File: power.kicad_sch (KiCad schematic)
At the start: 0 parts

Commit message: added symbols
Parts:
- added U4: ~, symbol sumo-robot-symbols:RS3E075AT
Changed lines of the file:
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@@
 	(generator_version "9.0")
 	(paper "A4")
+	(symbol
+		(lib_id "sumo-robot-symbols:RS3E075AT")
+		(at 129.54 82.55 0)
+		(unit 1)
+		(exclude_from_sim no)
+		(in_bom yes)
+		(on_board yes)
+		(dnp no)
+		(property "Reference" "U4"
+			(at 130.302 69.596 0)
+			(effects
+				(font
+					(size 1.27 1.27)
+				)
+			)
+		)
+		(property "Value" "~"
+			(at 137.16 67.31 0)
+			(effects
+				(font
+					(size 1.27 1.27)
+				)
+			)
+		)
+		(property "Footprint" ""
+			(at 129.54 82.55 0)
+			(effects
+				(font
+					(size 1.27 1.27)
+				)
+				(hide yes)
+			)
+		)
+		(property "Datasheet" ""
+			(at 129.54 82.55 0)
+			(effects
+				(font
+					(size 1.27 1.27)
+				)
+				(hide yes)
+			)
+		)
+		(property "Description" ""
+			(at 129.54 82.55 0)
+			(effects
+				(font
+					(size 1.27 1.27)
+				)
+				(hide yes)
+			)
+		)
+		(pin "2"
+		)
+		(pin "3"
+		)
+		(pin "4"
+		)
+		(pin "8"
+		)
+		(pin "7"
+		)
+		(pin "6"
+		)
+		(pin "5"
+		)
+		(pin "1"
+		)
+		(instances
+			(project ""
+				(path "/f283bc71-7763-4093-b75c-cbe2f5868c12/4425b7fb-6f26-4a13-b5c2-41b1a59df573"
+					(reference "U4")
+					(unit 1)
+				)
+			)
+		)
+	)
 )

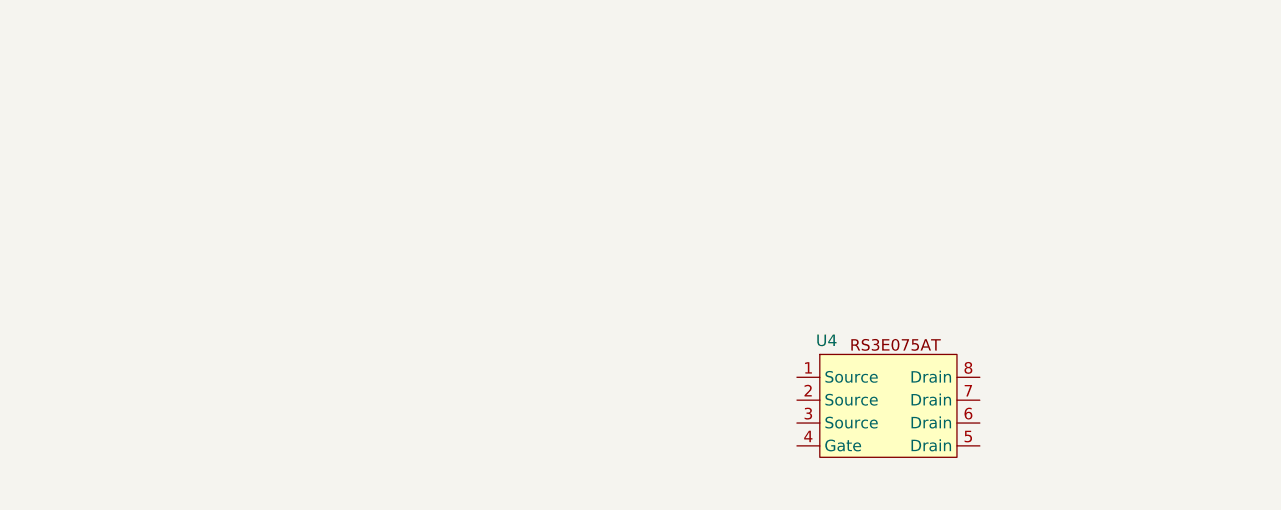
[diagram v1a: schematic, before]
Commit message: added power connectors and modified power shematic
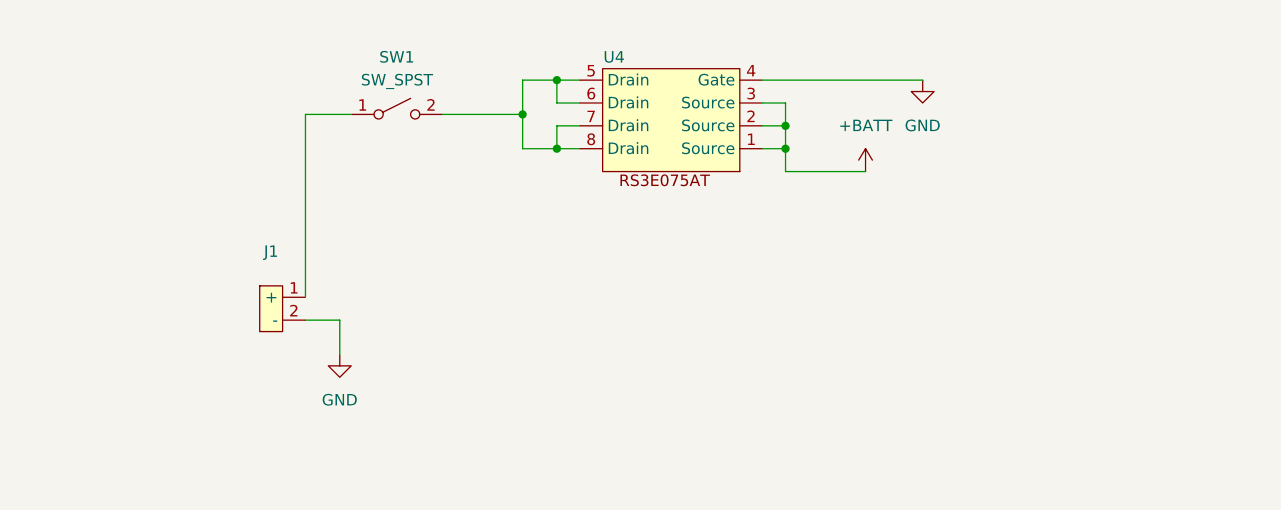
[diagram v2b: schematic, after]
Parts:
- added J1: ~, symbol sumo-robot-symbols:Mini-TRA-Receptacle
- added SW1: SW_SPST, Button_Switch_SMD:SW_MEC_5GSH9, symbol Switch:SW_SPST
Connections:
- net +BATT: now reaches U4.1 (Source)
- net +BATT: now also U4.2 (Source), U4.3 (Source)
- net GND: now reaches U4.4 (Gate)
- net GND: now also J1.2 (-)
- net at U4.5 (Drain): now also U4.6 (Drain), U4.7 (Drain), U4.8 (Drain), SW1.2 (B)
- new net: J1.1 (+), SW1.1 (A)
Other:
- moved on the sheet: U4

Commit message: updated poer and range sensor scheamtics
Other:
- moved on the sheet: J1, SW1, U4

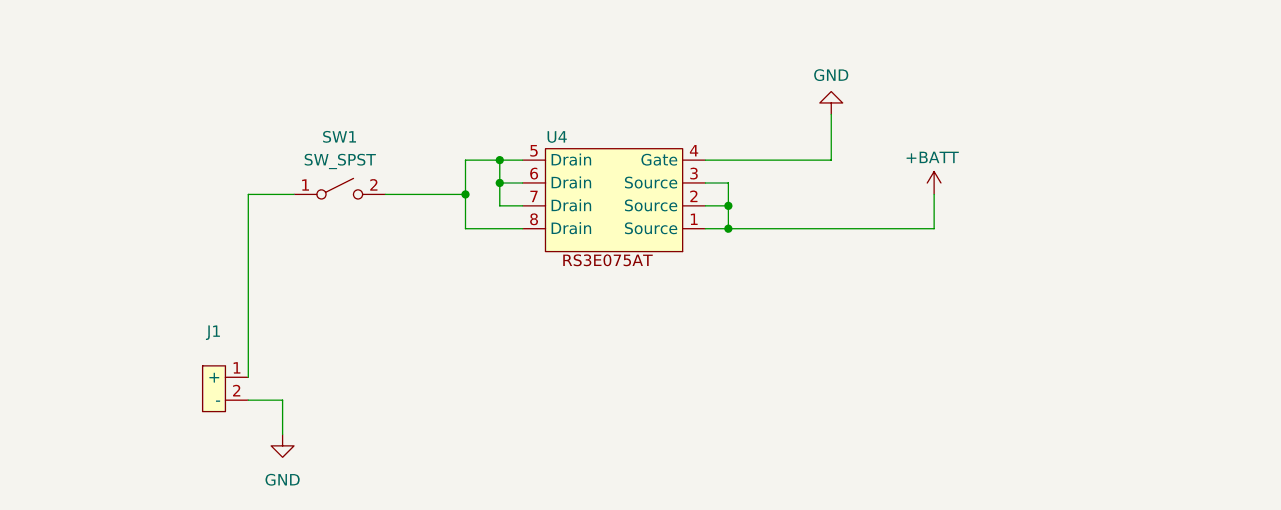
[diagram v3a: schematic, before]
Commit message: added LDO
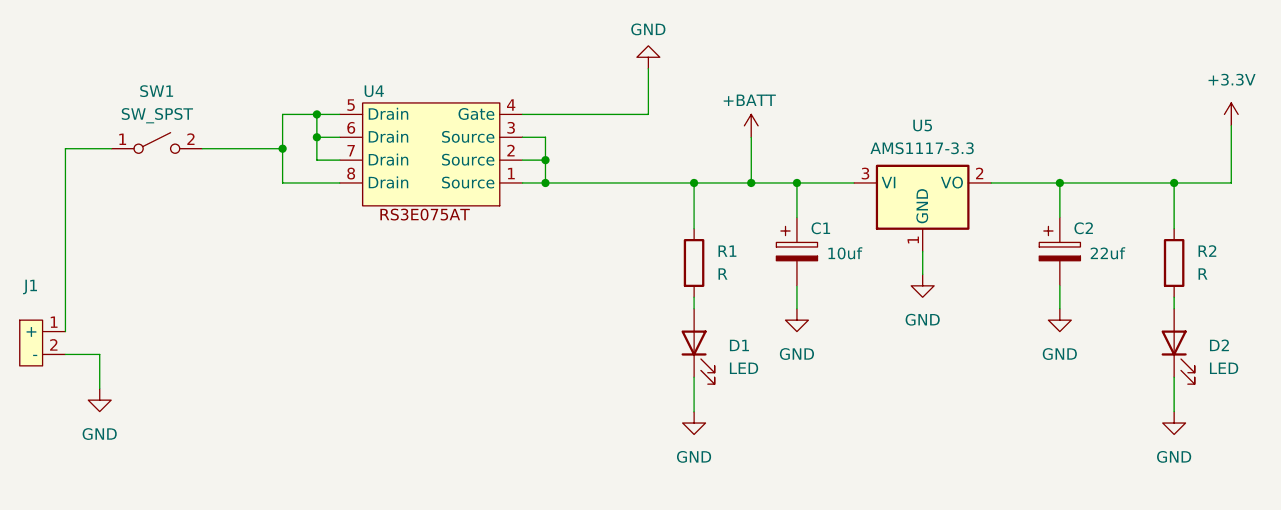
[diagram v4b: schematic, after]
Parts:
- added C1: 10uf, symbol Device:C_Polarized
- added C2: 22uf, symbol Device:C_Polarized
- added D1, D2: LED, LED_SMD:LED_1210_3225Metric, symbol Device:LED
- added R1, R2: R, Resistor_SMD:R_1210_3225Metric, symbol Device:R
- added U5: AMS1117-3.3, Package_TO_SOT_SMD:SOT-223-3_TabPin2, symbol Regulator_Linear:AMS1117-3.3
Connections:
- net +BATT: now also C1.1, R1.1, U5.3 (VI)
- net GND: now also C1.2, C2.2, D1.1 (K), D2.1 (K), U5.1 (GND)
- new net: D1.2 (A), R1.2
- new net: D2.2 (A), R2.2
- new net +3.3V: C2.1, R2.1, U5.2 (VO)
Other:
- moved on the sheet: J1, SW1, U4

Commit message: added more details to schematics
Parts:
- R1: value R -> 3k
- R2: value R -> 1k
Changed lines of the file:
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@@
 			)
 		)
-		(property "Value" "R"
+		(property "Value" "1k"
 			(at 171.45 62.2299 0)
 			(effects
@@
 			)
 		)
-		(property "Value" "R"
+		(property "Value" "3k"
 			(at 118.11 62.2299 0)
 			(effects

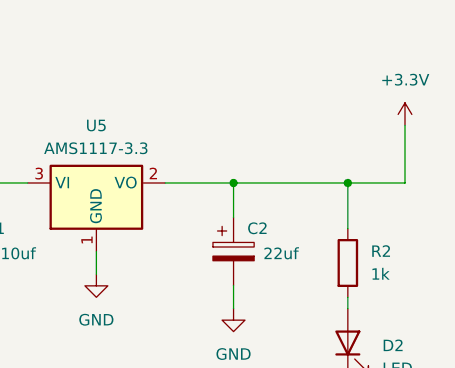
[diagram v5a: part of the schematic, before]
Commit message: started adding DC Motor controller logic
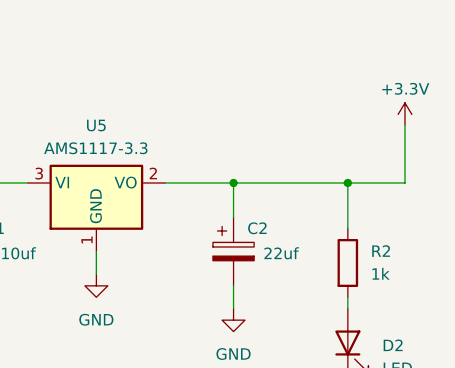
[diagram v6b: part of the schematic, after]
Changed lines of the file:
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@@
 		(on_board yes)
 		(dnp no)
-		(fields_autoplaced yes)
 		(property "Reference" "#PWR016"
 			(at 175.26 49.53 0)
@@
 		)
 		(property "Value" "+3.3V"
-			(at 175.26 40.64 0)
+			(at 175.26 41.656 0)
 			(effects
 				(font

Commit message: added all footprints and step files to components
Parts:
- C1, C2: footprint (none) -> Capacitor_SMD:C_1210_3225Metric
- J1: footprint (none) -> Connector_AMASS:AMASS_XT60-F_1x02_P7.20mm_Vertical
- SW1: footprint Button_Switch_SMD:SW_MEC_5GSH9 -> Button_Switch_SMD:SW_DIP_SPSTx01_Slide_9.78x4.72mm_W8.61mm_P2.54mm
- U4: footprint (none) -> Package_SO:SOP-8_3.76x4.96mm_P1.27mm
- U5: footprint Package_TO_SOT_SMD:SOT-223-3_TabPin2 -> Package_TO_SOT_SMD:SOT-223
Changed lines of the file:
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@@
 			)
 		)
-		(property "Footprint" "Package_TO_SOT_SMD:SOT-223-3_TabPin2"
+		(property "Footprint" "Package_TO_SOT_SMD:SOT-223"
 			(at 140.97 46.99 0)
 			(effects
@@
 			)
 		)
-		(property "Footprint" ""
+		(property "Footprint" "Package_SO:SOP-8_3.76x4.96mm_P1.27mm"
 			(at 93.98 43.18 0)
 			(effects
@@
 			)
 		)
-		(property "Footprint" "Button_Switch_SMD:SW_MEC_5GSH9"
+		(property "Footprint" "Button_Switch_SMD:SW_DIP_SPSTx01_Slide_9.78x4.72mm_W8.61mm_P2.54mm"
 			(at 55.88 48.26 0)
 			(effects
@@
 			)
 		)
-		(property "Footprint" ""
+		(property "Footprint" "Capacitor_SMD:C_1210_3225Metric"
 			(at 127.9652 63.5 0)
 			(effects
@@
 			)
 		)
-		(property "Footprint" ""
+		(property "Footprint" "Capacitor_SMD:C_1210_3225Metric"
 			(at 157.1752 63.5 0)
 			(effects
@@
 			)
 		)
-		(property "Footprint" ""
+		(property "Footprint" "Connector_AMASS:AMASS_XT60-F_1x02_P7.20mm_Vertical"
 			(at 40.64 72.39 0)
 			(effects
